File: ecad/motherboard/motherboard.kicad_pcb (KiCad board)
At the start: 2 copper layers, 200 x 100 mm, 206 parts, among them J1 B6B-XH-A(LF)(SN), J2 Amphenol_10061913-xx0, J3 Amphenol_10061913-xx0, J4 Amphenol_10061913-xx0, J5 Amphenol_10061913-xx0, J6 Amphenol_10061913-xx0, J7 Amphenol_10061913-xx0, J8 Amphenol_10061913-xx0, J9 Amphenol_10061913-xx0, U1 CD4051BPWR4, U10 TLP4026G, U11 TLP4026G, U12 NE5532, U13 TLP4026G, U14 TLP4026G, U15 NE5532, U16 TLP4026G, U17 TLP4026G, U18 TCA9544APWR, U19 CD4051BPWR4, U2 NodeMCU ESP-32S, U20 CD4051BPWR4, U21 NE5532, U22 TLP4026G, U23 TLP4026G, U24 NE5532, U25 TLP4026G, U26 TLP4026G, U27 NE5532, U28 TLP4026G, U29 TLP4026G, U3 TCA9544APWR, U30 NE5532, U31 TLP4026G, U32 TLP4026G, U33 NE5532, U34 PGA231x, U4 CD4051BPWR4, U5 CD4051BPWR4, U6 NE5532, U7 TLP4026G, U8 TLP4026G, U9 NE5532

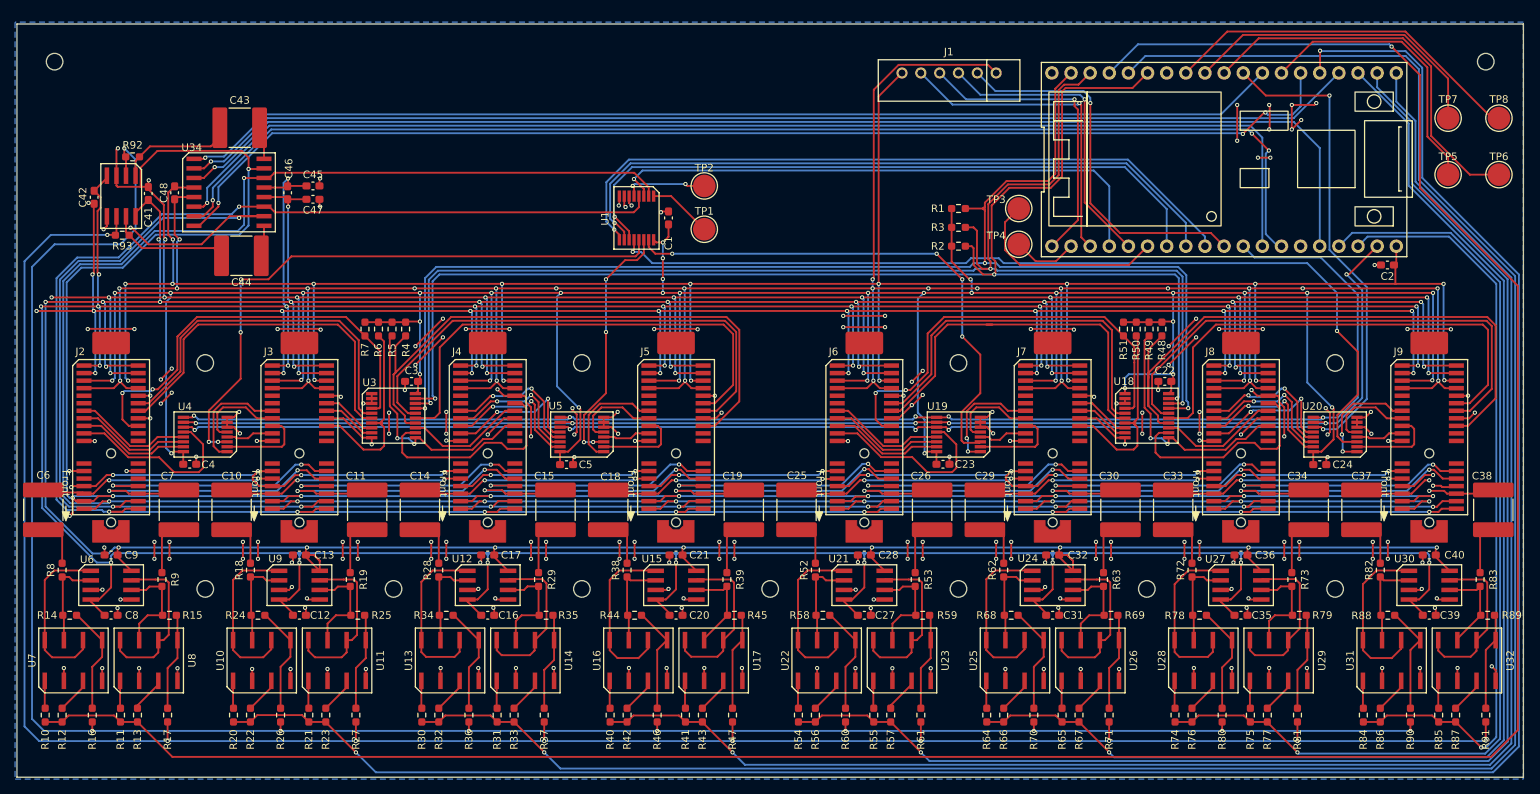
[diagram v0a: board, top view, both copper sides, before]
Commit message: Add new peripheral example board to better determine peripheral envelope and orientation in 3d space. Add several new parts to symbols, footprints, and 3dmodels
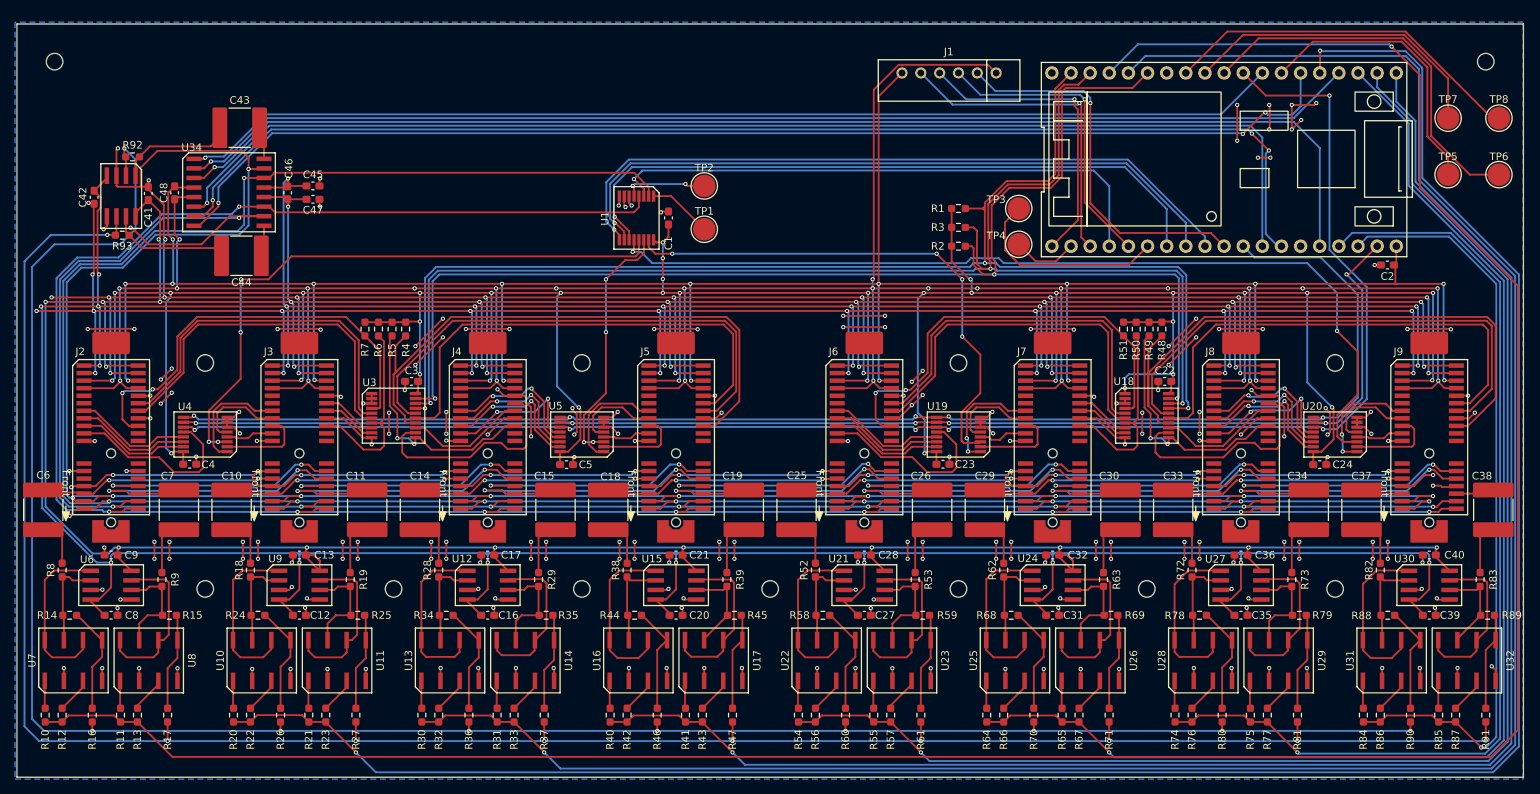
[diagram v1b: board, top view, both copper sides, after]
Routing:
- net /BP_4Board_Control_and_Connect2/L_POMI_4: track 9.94 -> 4.91 mm, vias 1 -> 0
- net /BP_4Board_Control_and_Connect2/R_POMI_4: track 8.86 -> 4.41 mm, vias 1 -> 0
- net +12V: track 580.1 -> 576.7 mm
- net Net-(C6-Pad1): track 6.68 -> 3.92 mm
- net Net-(C25-Pad1): track 6.68 -> 3.92 mm
- net Net-(C37-Pad1): track 6.74 -> 4.09 mm
- net Net-(C18-Pad1): track 6.74 -> 4.09 mm
- net Net-(C15-Pad1): track 7.44 -> 4.84 mm
- net Net-(C11-Pad1): track 7.44 -> 4.84 mm
- net Net-(C34-Pad1): track 7.44 -> 4.84 mm
- net Net-(C30-Pad1): track 7.44 -> 4.84 mm
- net -12V: track 610.4 -> 608.7 mm
- net Net-(C14-Pad1): track 6.44 -> 4.81 mm
- net Net-(C10-Pad1): track 6.53 -> 4.89 mm
- net Net-(C33-Pad1): track 6.44 -> 4.81 mm
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
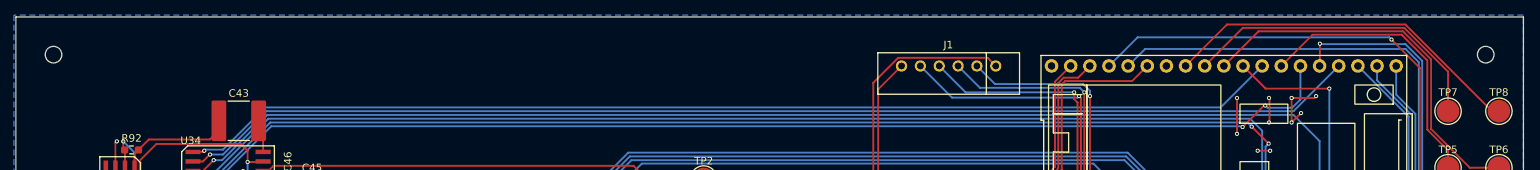
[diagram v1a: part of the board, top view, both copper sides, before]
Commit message: Small changes and cleanup as 3dmodels are pieced together.
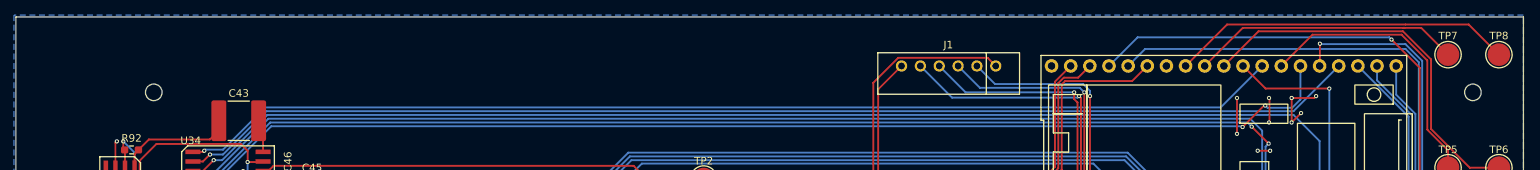
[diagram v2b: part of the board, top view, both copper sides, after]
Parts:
- moved REF** 14.2 mm to (75.8, 60.5)
- moved TP7 7.50 mm to (247.5, 55.5)
- moved TP8 7.50 mm to (254.2, 55.5)
- moved REF** 5.28 mm to (250.8, 60.5)
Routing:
- net Net-(U2-IO18/I2S_DOUT): track 42.0 -> 36.0 mm
- net Net-(U2-IO19/I2S_DIN): track 47.7 -> 45.5 mm

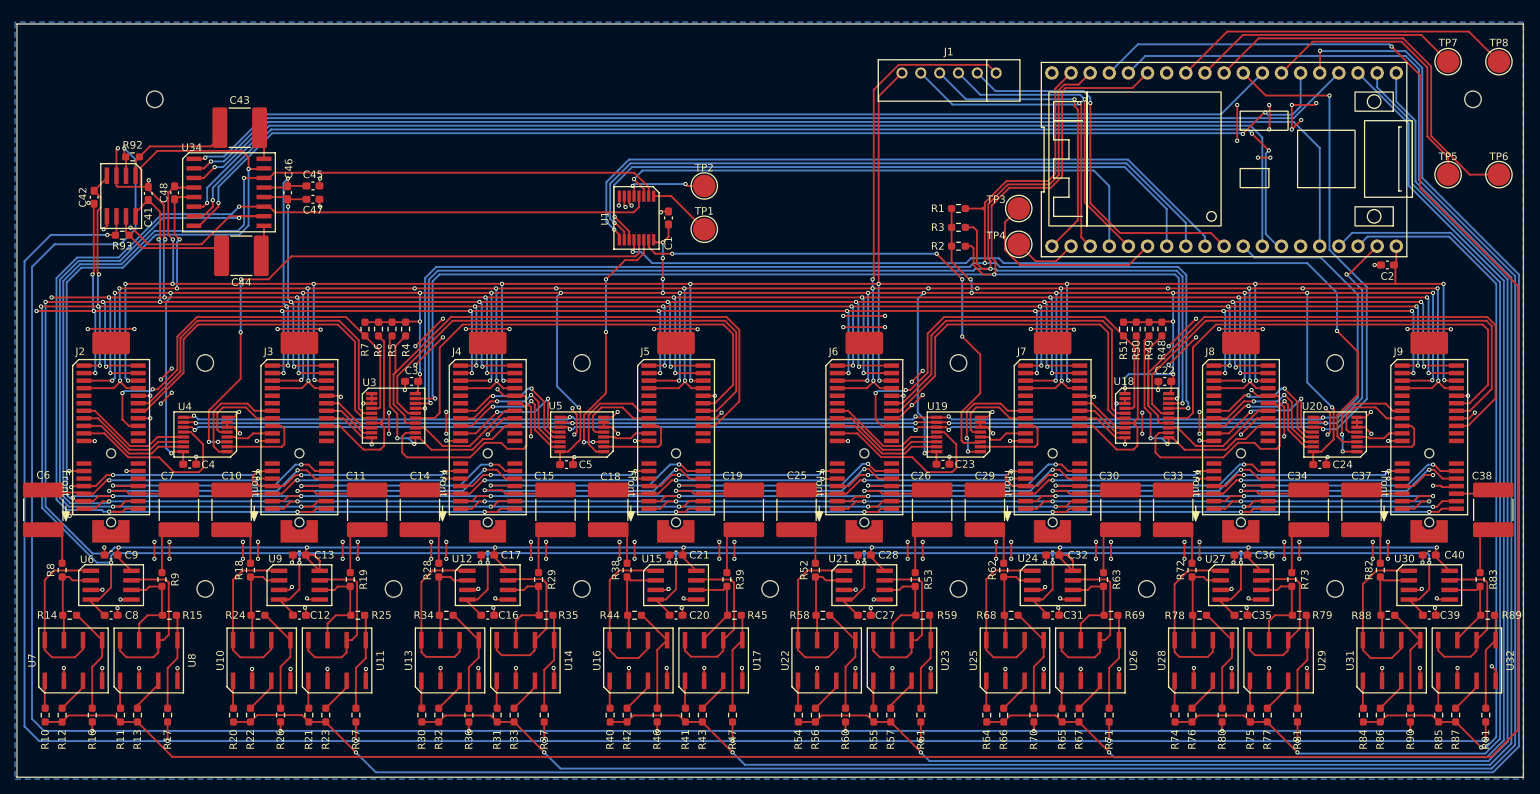
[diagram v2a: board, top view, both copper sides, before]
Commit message: Good state for mechanical assembly, can bounce back to pcb review now that board outlines are close.
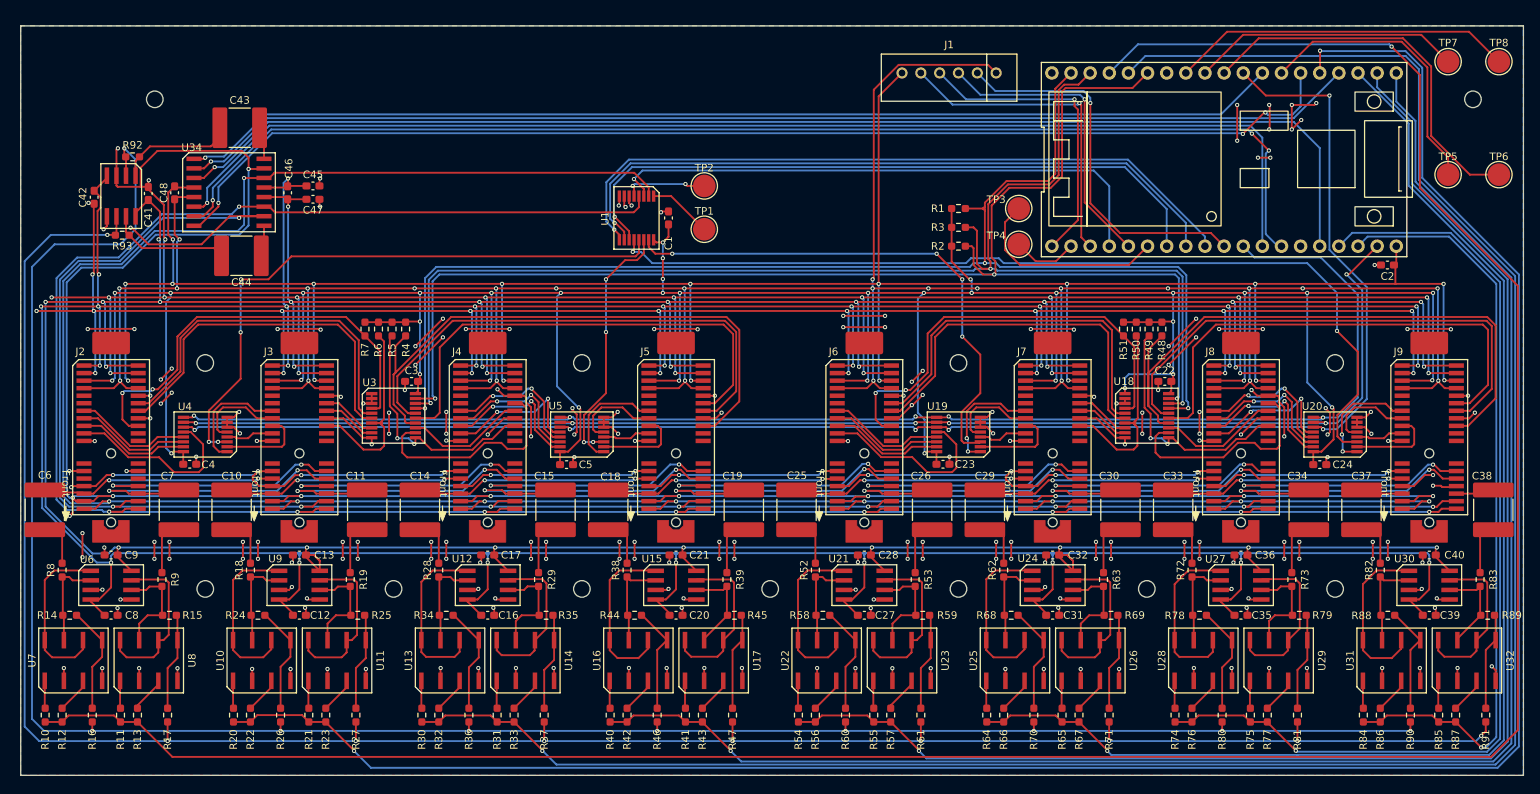
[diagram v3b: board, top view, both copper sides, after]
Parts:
- moved C6 0.20 mm to (61.2, 115.0)
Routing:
- net GND: track 2416.5 -> 2419.7 mm, vias 340 -> 342
- net /BP_4Board_Control_and_Connect1/R_MSum: track 292.6 -> 291.9 mm
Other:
- board size 200 x 100 mm -> 199.5 x 99.5 mm

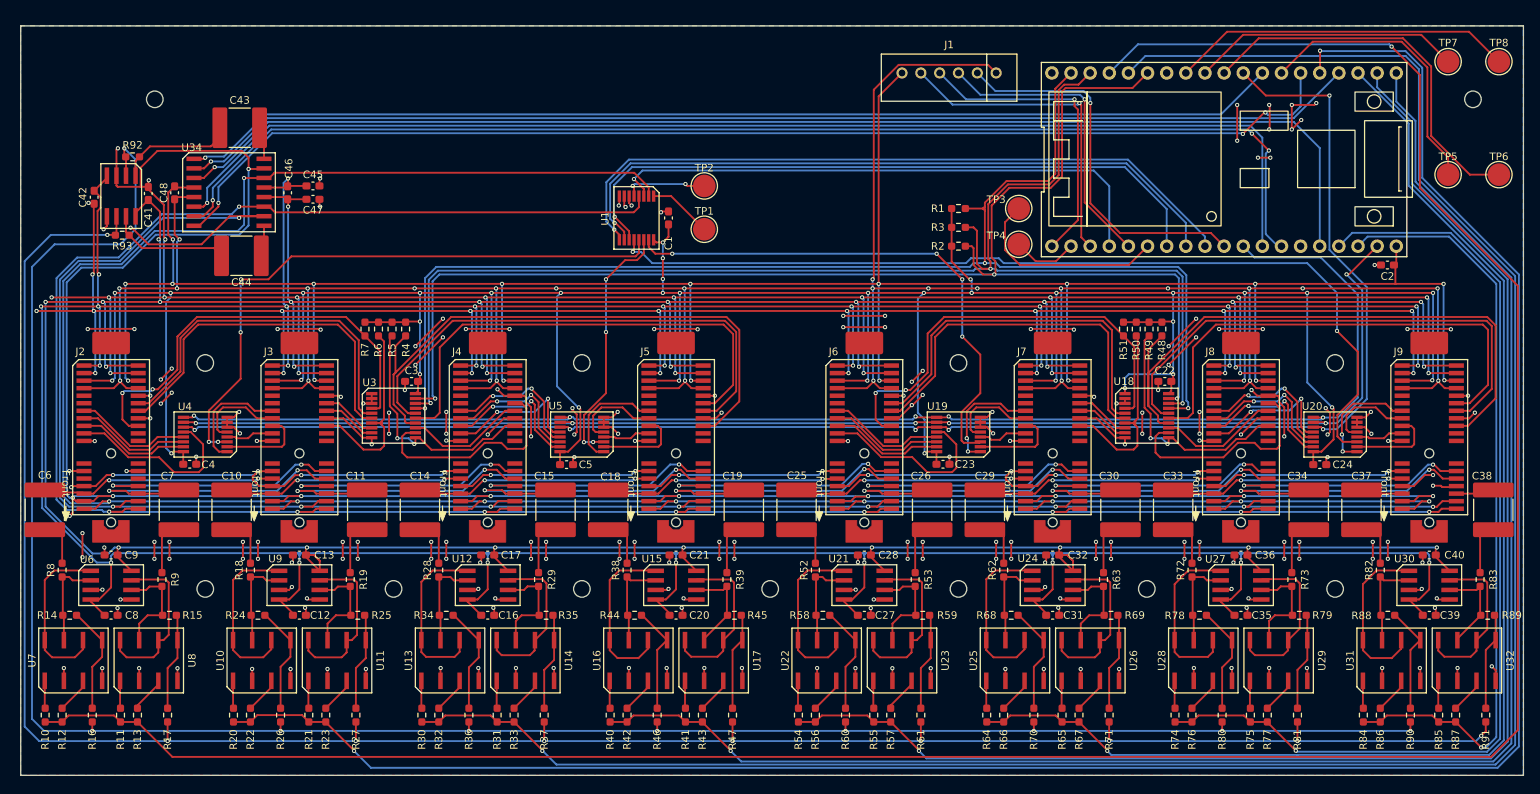
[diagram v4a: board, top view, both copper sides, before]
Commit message: Small tweaks to routing for better signal return paths. Fix minor footprint issues: missing courtyards, smt parts labeled as through hole.
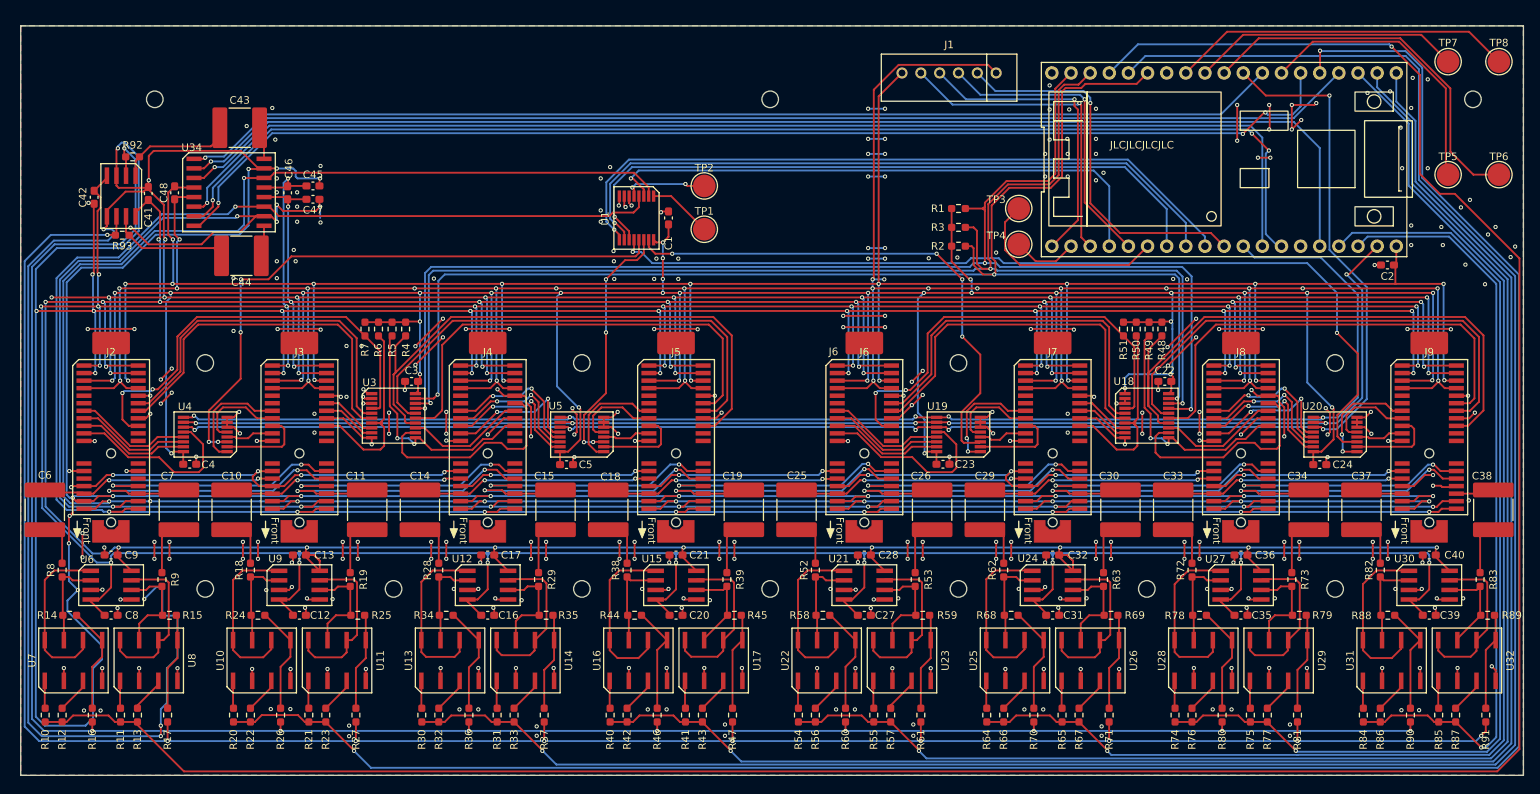
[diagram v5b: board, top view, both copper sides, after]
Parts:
- removed mainboard: Board, PCM_kikit:Board
- added REF**: MountingHole_2.2mm_M2, MountingHole:MountingHole_2.2mm_M2, F.Cu at (157.5, 60.5)
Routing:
- net GND: track 2419.7 -> 2712.7 mm, vias 342 -> 482
- net /~{Mute_CH1}: track 336.5 -> 341.3 mm
- net /BP_4Board_Control_and_Connect2/Channel4/I2C_SCL: track 69.2 -> 66.0 mm
- net /BP_4Board_Control_and_Connect2/Channel4/I2C_SDA: track 65.4 -> 62.2 mm
- net /BP_4Board_Control_and_Connect2/Channel4/I2C_INT: track 84.5 -> 81.5 mm
- net /BP_4Board_Control_and_Connect1/Channel4/I2C_SDA: track 64.7 -> 62.4 mm
- net /BP_4Board_Control_and_Connect1/Channel4/I2C_SCL: track 68.5 -> 66.4 mm
- net /BP_4Board_Control_and_Connect1/Channel4/I2C_INT: track 79.5 -> 77.7 mm
- net /~{I2C_INT}: track 177.7 -> 179.2 mm
- net /ID_COM: track 75.2 -> 76.0 mm
- net /I2C_SDA: track 185.9 -> 185.1 mm
- net /L_MOPI: vias 9 -> 10
- added copper zone on F.Cu, net GND
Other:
- board text added: "JLCJLCJLCJLC"

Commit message: Add silkscreen markings.
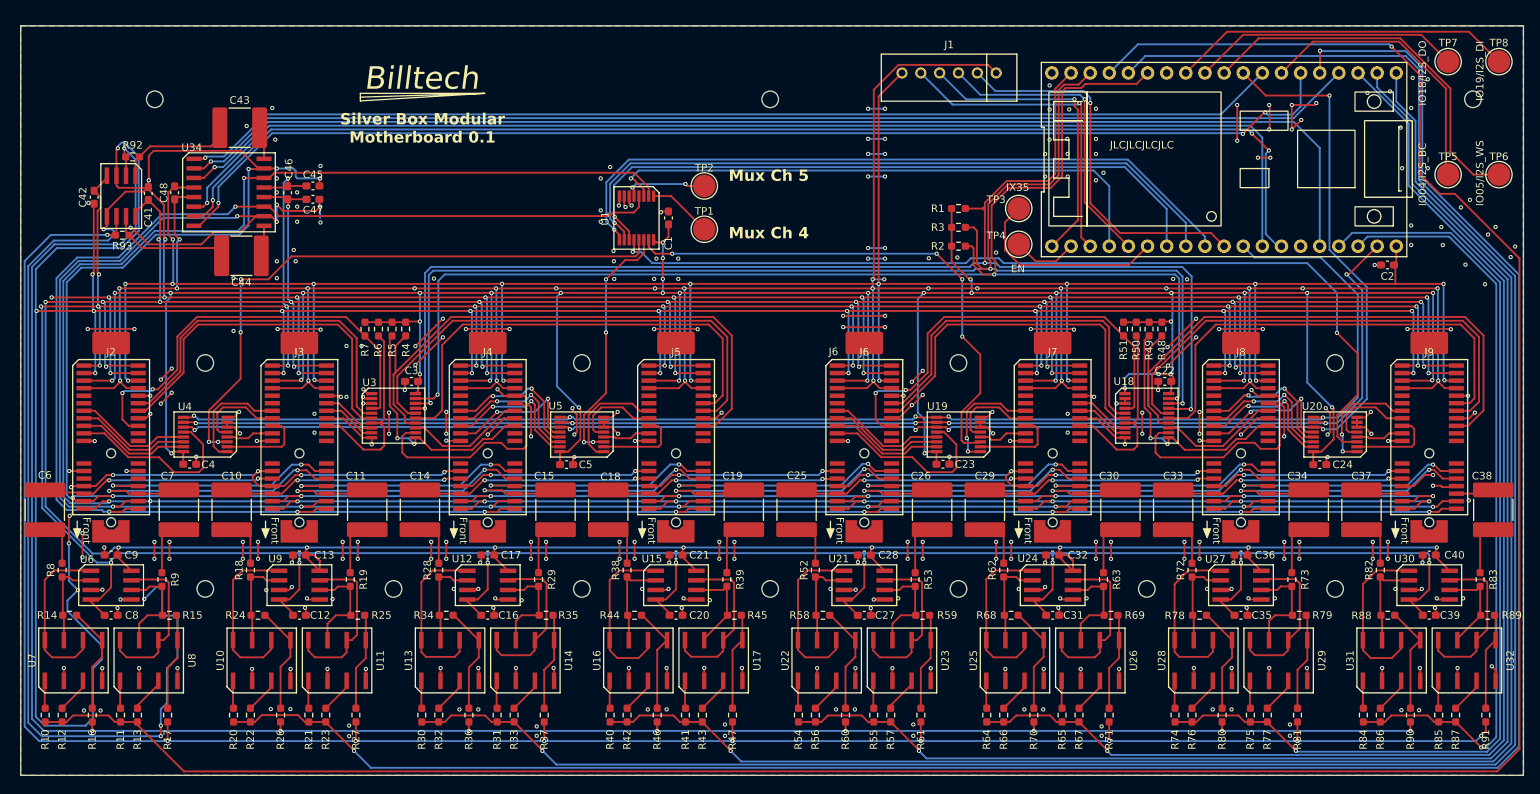
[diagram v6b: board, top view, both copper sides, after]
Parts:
- added REF**: Billtech, silver-box-feetprints:Billtech, F.Cu at (112.0, 58.0)
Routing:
- net +3V3: vias 37 -> 38
- net GND: vias 482 -> 483
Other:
- board text added: "EN"
- board text added: "IO04/I2S_BC"
- board text added: "IO05/I2S_WS"
- board text added: "IO18/I2S_DO"
- board text added: "IO19/I2S_DI"
- board text added: "IX35"
- board text added: "Mux Ch 4"
- board text added: "Mux Ch 5"
- board text added: "Silver Box Modular Motherboard 0.1"
